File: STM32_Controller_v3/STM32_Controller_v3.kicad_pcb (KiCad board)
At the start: 2 copper layers, 100 x 80 mm, 168 parts, among them CN1 WJ15EDGVC-3.5-09P-14-00A, CN10 DS1021-1x5SF11-B, CN2 WJ15EDGVC-3.5-05P-14-00A, CN3 WJ15EDGVC-3.5-02P-14-00A, CN8 DS1021-1x4SF11-B, CN9 DS1021-1x6SF11-B, Q1 SMMBT5551LT1G, Q10 SMMBT5551LT1G, Q11 SMMBT5551LT1G, Q12 SMMBT5551LT1G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

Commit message: production version
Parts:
- added H1: MountingHole, Library:MountingHole_4.3mm_M4_Pad_Via, F.Cu at (53.5, 74.5)
- added H2: MountingHole, Library:MountingHole_4.3mm_M4_Pad_Via, F.Cu at (53.5, 145.5)
- added H3: MountingHole, Library:MountingHole_4.3mm_M4_Pad_Via, F.Cu at (144.5, 145.5)
- added H4: MountingHole, Library:MountingHole_4.3mm_M4_Pad_Via, F.Cu at (144.5, 74.5)
- C10, C9: footprint db_capacitors:C_1206 -> Library:C_1206
- C11: footprint db_capacitors:C_0805 -> Library:C_0805
- CN1: value WJ15EDGVC-3.5-09P-14-00A -> WJ15EDGVC-3.81-09P-14-00A; footprint Library:PhoenixContact_MCV_1,5_9-G-3.5_1x09_P3.50mm_Vertical -> Library:PhoenixContact_MCV_1,5_9-G-3.81_1x09_P3.81mm_Vertical
- CN2: value WJ15EDGVC-3.5-05P-14-00A -> WJ15EDGVC-3.81-05P-14-00A; footprint Library:PhoenixContact_MCV_1,5_5-G-3.5_1x05_P3.50mm_Vertical -> Library:PhoenixContact_MCV_1,5_5-G-3.81_1x05_P3.81mm_Vertical
- CN3: value WJ15EDGVC-3.5-02P-14-00A -> WJ15EDGVC-3.81-02P-14-00A; footprint Library:PhoenixContact_MCV_1,5_2-G-3.5_1x02_P3.50mm_Vertical -> Library:PhoenixContact_MCV_1,5_2-G-3.81_1x02_P3.81mm_Vertical
- moved R67 25.7 mm to (137.0, 88.0)
- moved CN10 25.1 mm to (143.0, 93.3)
- moved R66 24.0 mm to (137.0, 84.5)
- moved R68 24.0 mm to (137.0, 82.5)
- moved R73 24.0 mm to (137.0, 93.5)
- moved R65 22.0 mm to (137.0, 90.5)
- moved G1 19.4 mm to (116.0, 99.5)
- moved FD1 18.6 mm to (133.5, 80.0)
- moved Q14 11.7 mm to (126.0, 86.0)
- moved R72 11.5 mm to (122.0, 85.5), turned to 0 degrees
- moved R75 9.62 mm to (128.5, 92.0), turned to 90 degrees
- moved R74 9.18 mm to (125.0, 92.0), turned to 90 degrees
- moved FD2 4.37 mm to (62.0, 146.2)
- moved Q13 4.00 mm to (108.0, 88.5)
- moved R62 4.00 mm to (108.0, 84.5)
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- renumbered G*** to G1
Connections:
- net Net-(D10-K) renamed /Power_Supply/TPS_PH
- net Net-(U1-BOOT) renamed /Power_Supply/TPS_BOOT
- net Net-(U1-VIN) renamed /Power_Supply/TPS_VIN
- net Net-(U1-VSENSE) renamed /Power_Supply/TPS_FB
- R83 pad 2: +3.3V -> +3.3V_P
- U3 pad 2: unconnected-(U3-PC13-Pad2) -> /Mcu_Stm32/LCD_BKL
- U3 pad 38: /Mcu_Stm32/LCD_BKL -> unconnected-(U3-PA15-Pad38)
- U3 pad 39: /Mcu_Stm32/LCD_D7 -> /Mcu_Stm32/LCD_RS
- U3 pad 40: /Mcu_Stm32/LCD_D6 -> /Mcu_Stm32/LCD_RW
- U3 pad 41: /Mcu_Stm32/LCD_D5 -> /Mcu_Stm32/LCD_E
- U3 pad 43: /Mcu_Stm32/LCD_E -> /Mcu_Stm32/LCD_D5
- U3 pad 45: /Mcu_Stm32/LCD_RW -> /Mcu_Stm32/LCD_D6
- U3 pad 46: /Mcu_Stm32/LCD_RS -> /Mcu_Stm32/LCD_D7
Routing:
- net +3.3V: track 0.00 -> 364.3 mm, vias 0 -> 3
- net +V_IN: track 0.00 -> 220.4 mm, vias 0 -> 5
- net GND: track 0.00 -> 154.3 mm, vias 24 -> 111
- net +5V: track 0.00 -> 139.1 mm
- net +VLCD: track 0.00 -> 86.6 mm
- net +V_MCU: track 0.00 -> 65.2 mm, vias 0 -> 2
- net /Mcu_Stm32/NRST: track 0.00 -> 64.3 mm, vias 0 -> 4
- net /Mcu_Stm32/LCD_ON: track 0.00 -> 55.6 mm, vias 0 -> 2
- net /Mcu_Stm32/SWD_IO: track 0.00 -> 54.8 mm
- net /Mcu_Stm32/LCD_D4: track 0.00 -> 51.6 mm
- net /Mcu_Stm32/LCD_D5: track 0.00 -> 50.7 mm
- net /Mcu_Stm32/LCD_D6: track 0.00 -> 50.4 mm
- net /Mcu_Stm32/LCD_RS: track 0.00 -> 50.3 mm
- net /Mcu_Stm32/LCD_D7: track 0.00 -> 50.1 mm
- net /Mcu_Stm32/LCD_RW: track 0.00 -> 48.4 mm
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- added copper zone on F.Cu, net +5V_P
- added copper zone on F.Cu, net /Power_Supply/TPS_PH
- added copper zone on B.Cu, net GND
- added copper zone on F.Cu, net GND

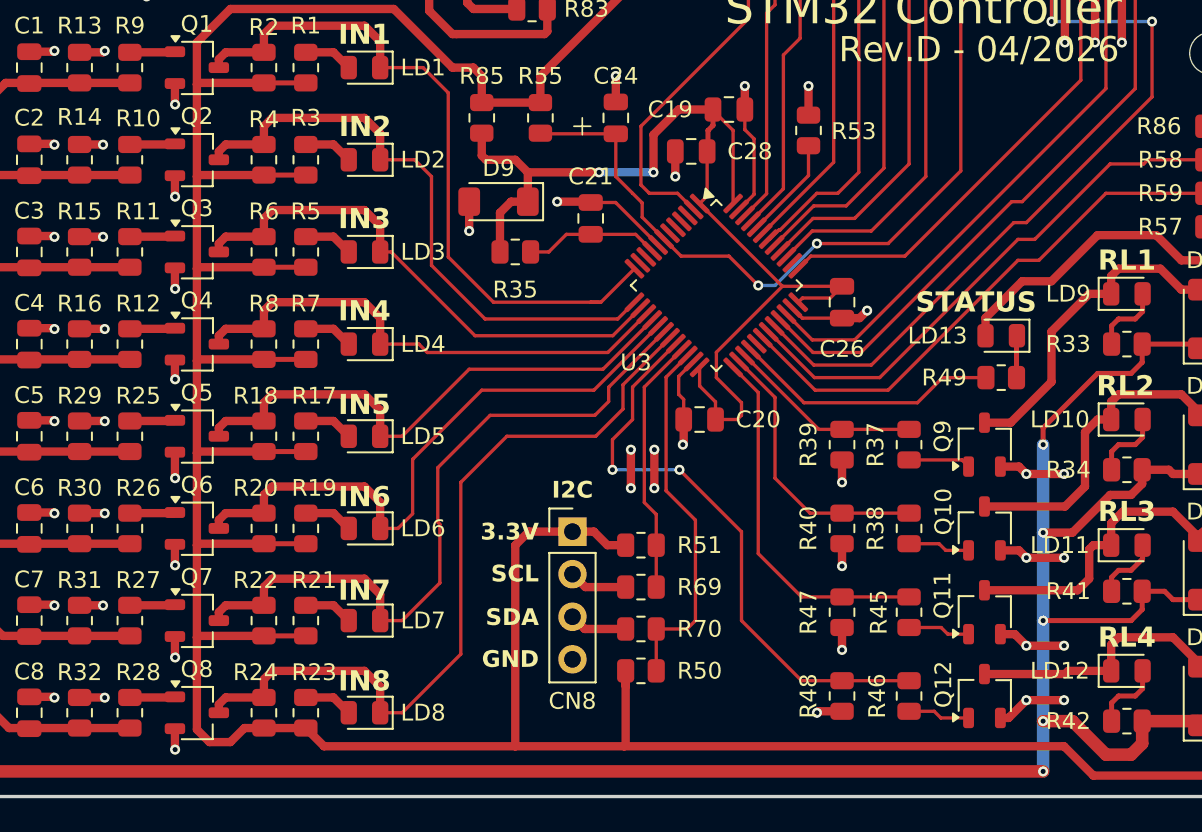
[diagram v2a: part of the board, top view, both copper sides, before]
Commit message: res 4k7 in digital inputs and outputs leds
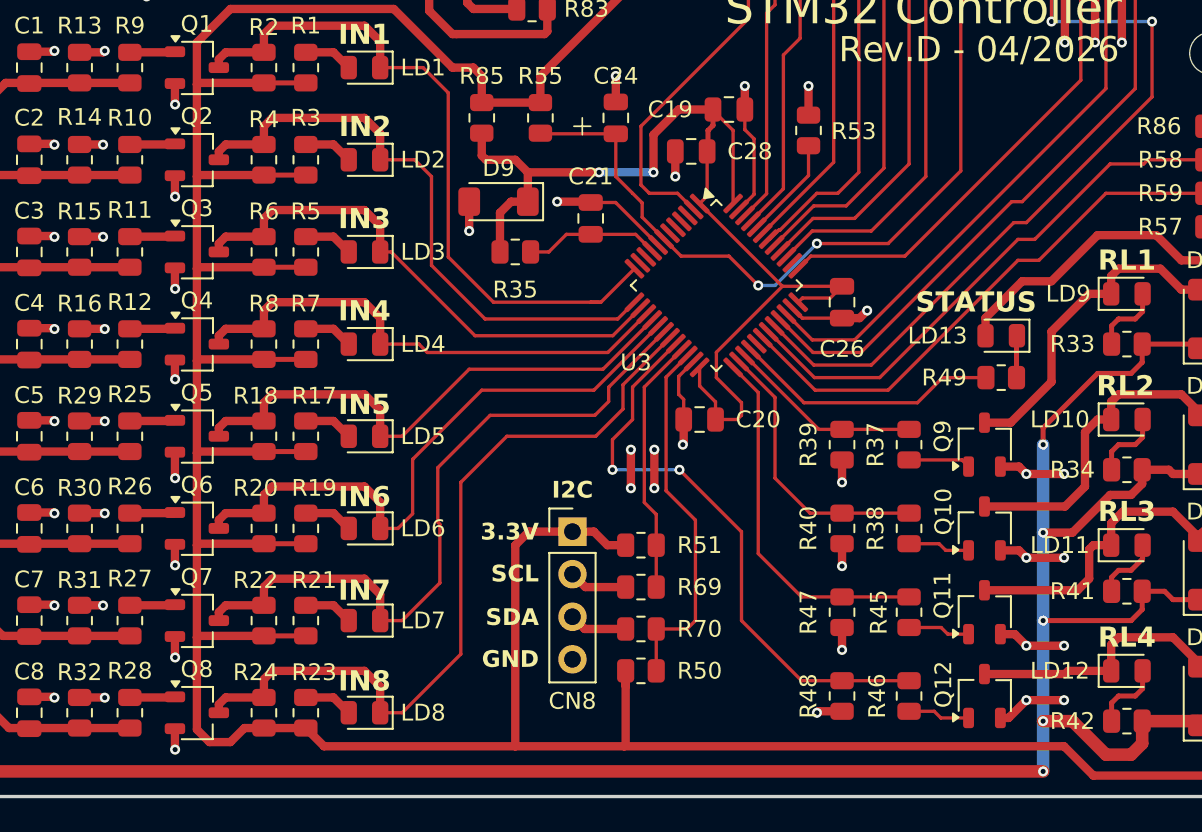
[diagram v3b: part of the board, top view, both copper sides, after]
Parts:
- L4: value FNR6045S220MT -> 22uF
- R10, R11, R12, R25, R26, R27, R28, R33, R34, R41, R42, R9: value 1K -> 4K7; footprint Library:R_0805 -> db_resistors:R_0805
- R36: value 1K -> 3K24
